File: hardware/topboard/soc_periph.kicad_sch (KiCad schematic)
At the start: 16 parts

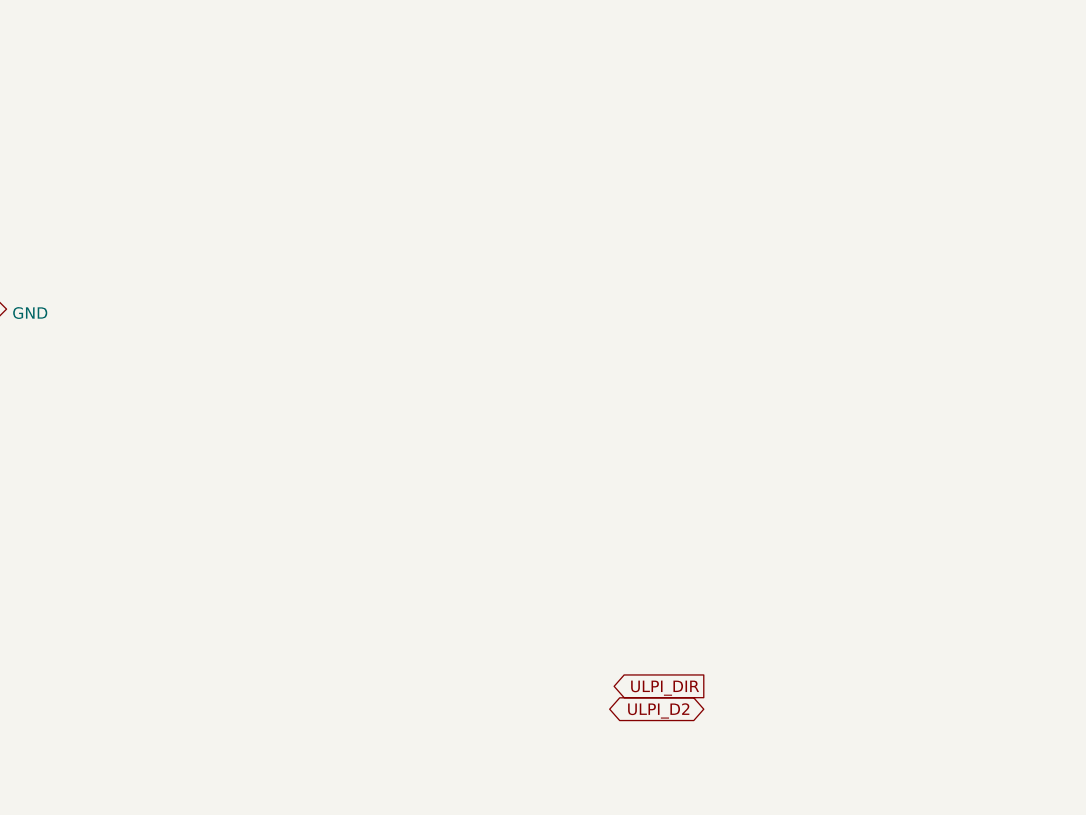
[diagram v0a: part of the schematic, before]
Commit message: Add PCIe and camera to front board
Signed-off-by: gatecat <gatecat@ds0.me>
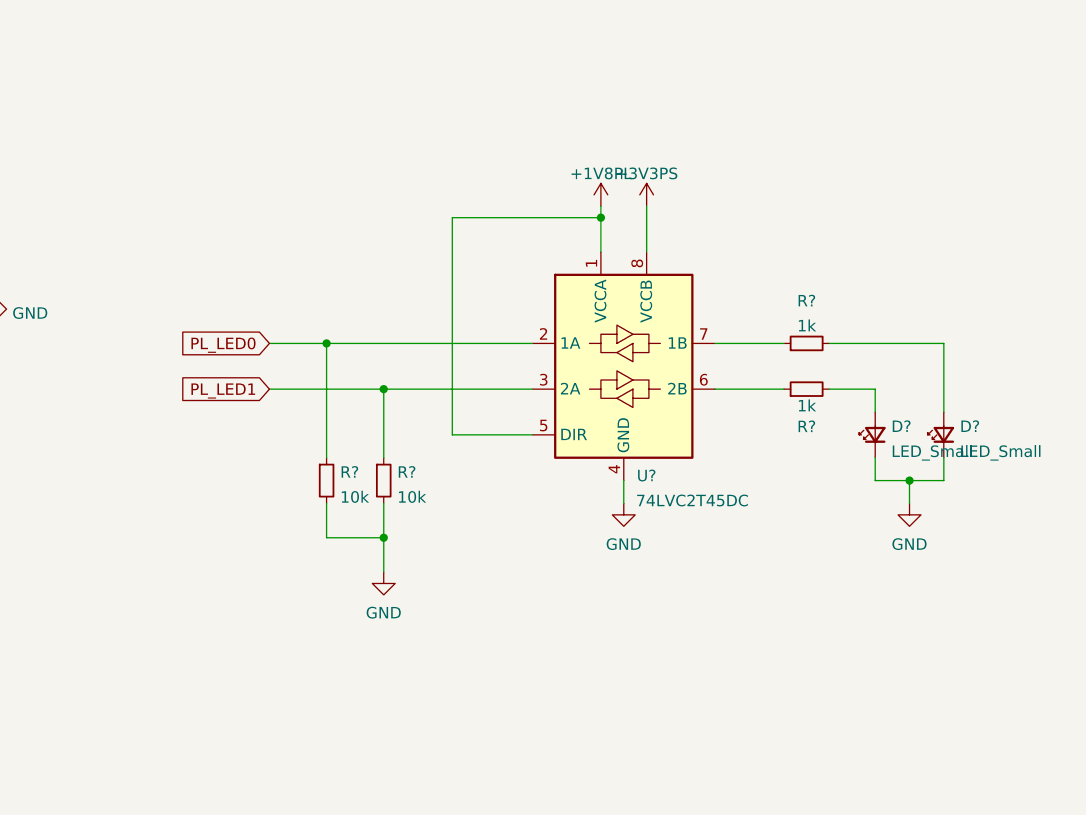
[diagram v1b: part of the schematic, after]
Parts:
- added D? (x2): LED_Small, symbol Device:LED_Small
- added R? (x2): 1k, symbol Device:R_Small
- added R? (x2): 10k, symbol Device:R_Small
- added U?: 74LVC2T45DC, Package_SO:VSSOP-8_2.3x2mm_P0.5mm, symbol Logic_LevelTranslator:74LVC2T45DC
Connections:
- net +3V3PS: now also U?.8 (VCCB)
- net GND: now also D?.1 (K), D?.1 (K), R?.2, R?.2, U?.4 (GND)
- new net: R?.1, U?.7 (1B)
- new net: D?.2 (A), R?.2 (x2)
- new net: R?.1, U?.6 (2B)
- new net +1V8PL: U?.1 (VCCA), U?.5 (DIR)
- new net PL_LED0: R?.1, U?.2 (1A)
- new net PL_LED1: R?.1, U?.3 (2A)

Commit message: Add IMU
Signed-off-by: gatecat <gatecat@ds0.me>
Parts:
- removed D? (x2): LED_Small, symbol Device:LED_Small
- removed R? (x2): 1k, symbol Device:R_Small
- removed R? (x2): 10k, symbol Device:R_Small
- removed U?: 74LVC2T45DC, Package_SO:VSSOP-8_2.3x2mm_P0.5mm, symbol Logic_LevelTranslator:74LVC2T45DC
- added C? (x3): 100n, symbol Device:C_Small
- added C?: 1µ, symbol Device:C_Small
- added D? (x7): LED_Small, symbol Device:LED_Small
- added Q? (x8): BSS138, Package_TO_SOT_SMD:SOT-23, symbol Transistor_FET:BSS138
- added R? (x11): 2.2k, symbol Device:R_Small
- added R? (x8): 10k, symbol Device:R_Small
- added U?: ICM-20789, symbol meowality:ICM-20789
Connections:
- net +1V8PL: now also R?.2
- net +1V8PS: now also C?.1, C?.1, C?.1, R?.1, R?.1, R?.2, R?.2, U?.13 (V_{DD}), U?.8 (V_{DDIO})
- net GND: now also C?.1, C?.2, C?.2, C?.2, Q?.2 (S), Q?.2 (S), Q?.2 (S), Q?.2 (S), Q?.2 (S), Q?.2 (S), Q?.2 (S), Q?.2 (S), R?.2, R?.2, R?.2, R?.2, R?.2, R?.2, R?.2, U?.18 (GND)
- net PL_LED0: now also Q?.1 (G), R?.1
- net PL_LED1: now also Q?.1 (G), R?.1
- new net: D?.2 (A), R?.1 (x7)
- new net: C?.2, U?.10 (REGOUT)
- new net: D?.1 (K), Q?.3 (D) (x7)
- new net +5V: R?.2, R?.2, R?.2, R?.2, R?.2, R?.2, R?.2
- new net I2C1_SCL: R?.2, U?.7 (PR_CL)
- new net I2C1_SDA: R?.2, U?.6 (PR_DA)
- new net IMU_FSYNC: U?.11 (FSYNC)
- new net IMU_INT: Q?.3 (D), R?.1
- new net IMU_INT_PS: Q?.1 (G), R?.1, U?.12 (INT)
- new net PS_ERR_OUT: Q?.1 (G), R?.1
- new net PS_ERR_STAT: Q?.1 (G), R?.1
- new net PS_LED: Q?.1 (G), R?.1
- new net SPI_C2M: U?.9 (AD0/SDO)
- new net SPI_M2C: U?.24 (SDA/SDI)
- new net SPI_SCLK: U?.23 (SCL/SCLK)
- new net SPI_~{CS}: R?.1, U?.22 (~{CS})
- new net VccO_EN_PL: Q?.1 (G), R?.1
- new net VccO_EN_PS: Q?.1 (G), R?.1
- no-connect marks 10 -> 18

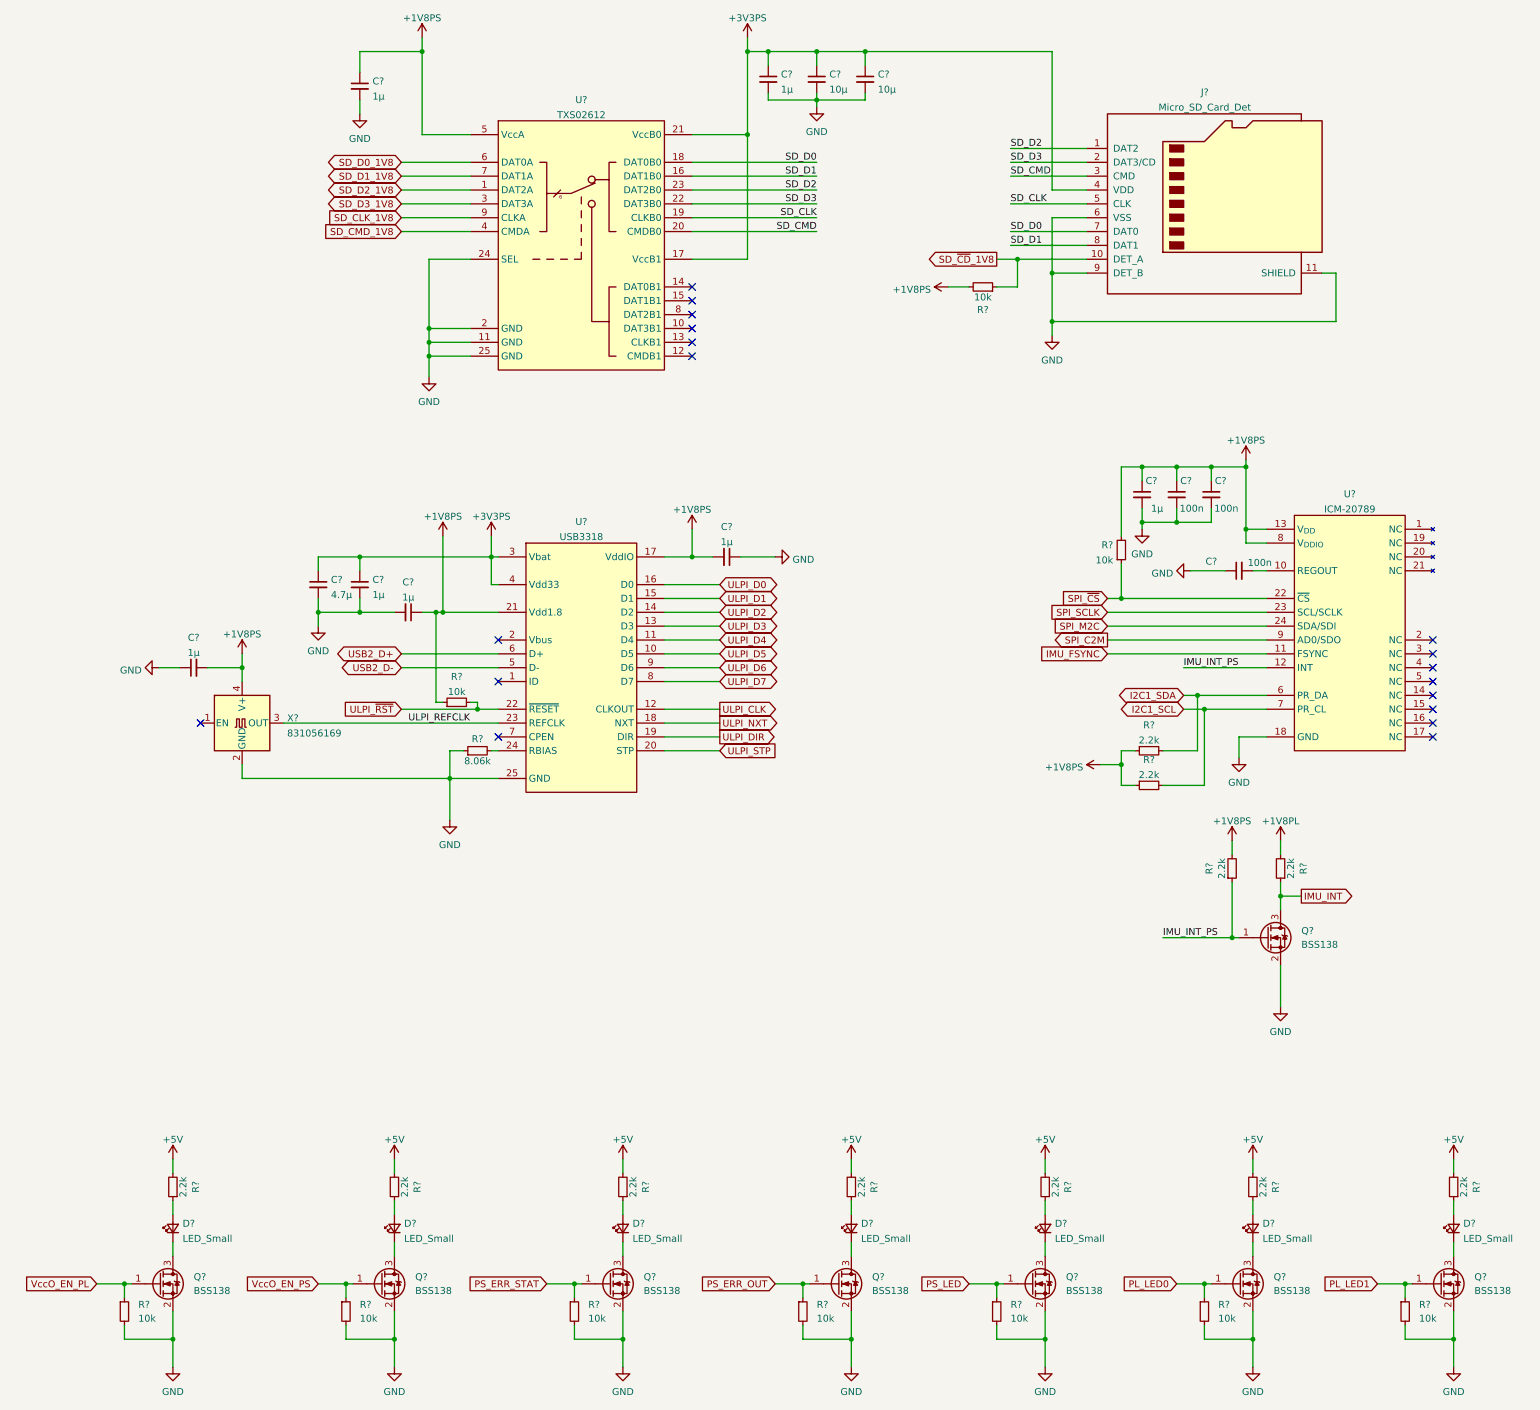
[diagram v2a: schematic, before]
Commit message: Fixing various top board issues
Signed-off-by: gatecat <gatecat@ds0.me>
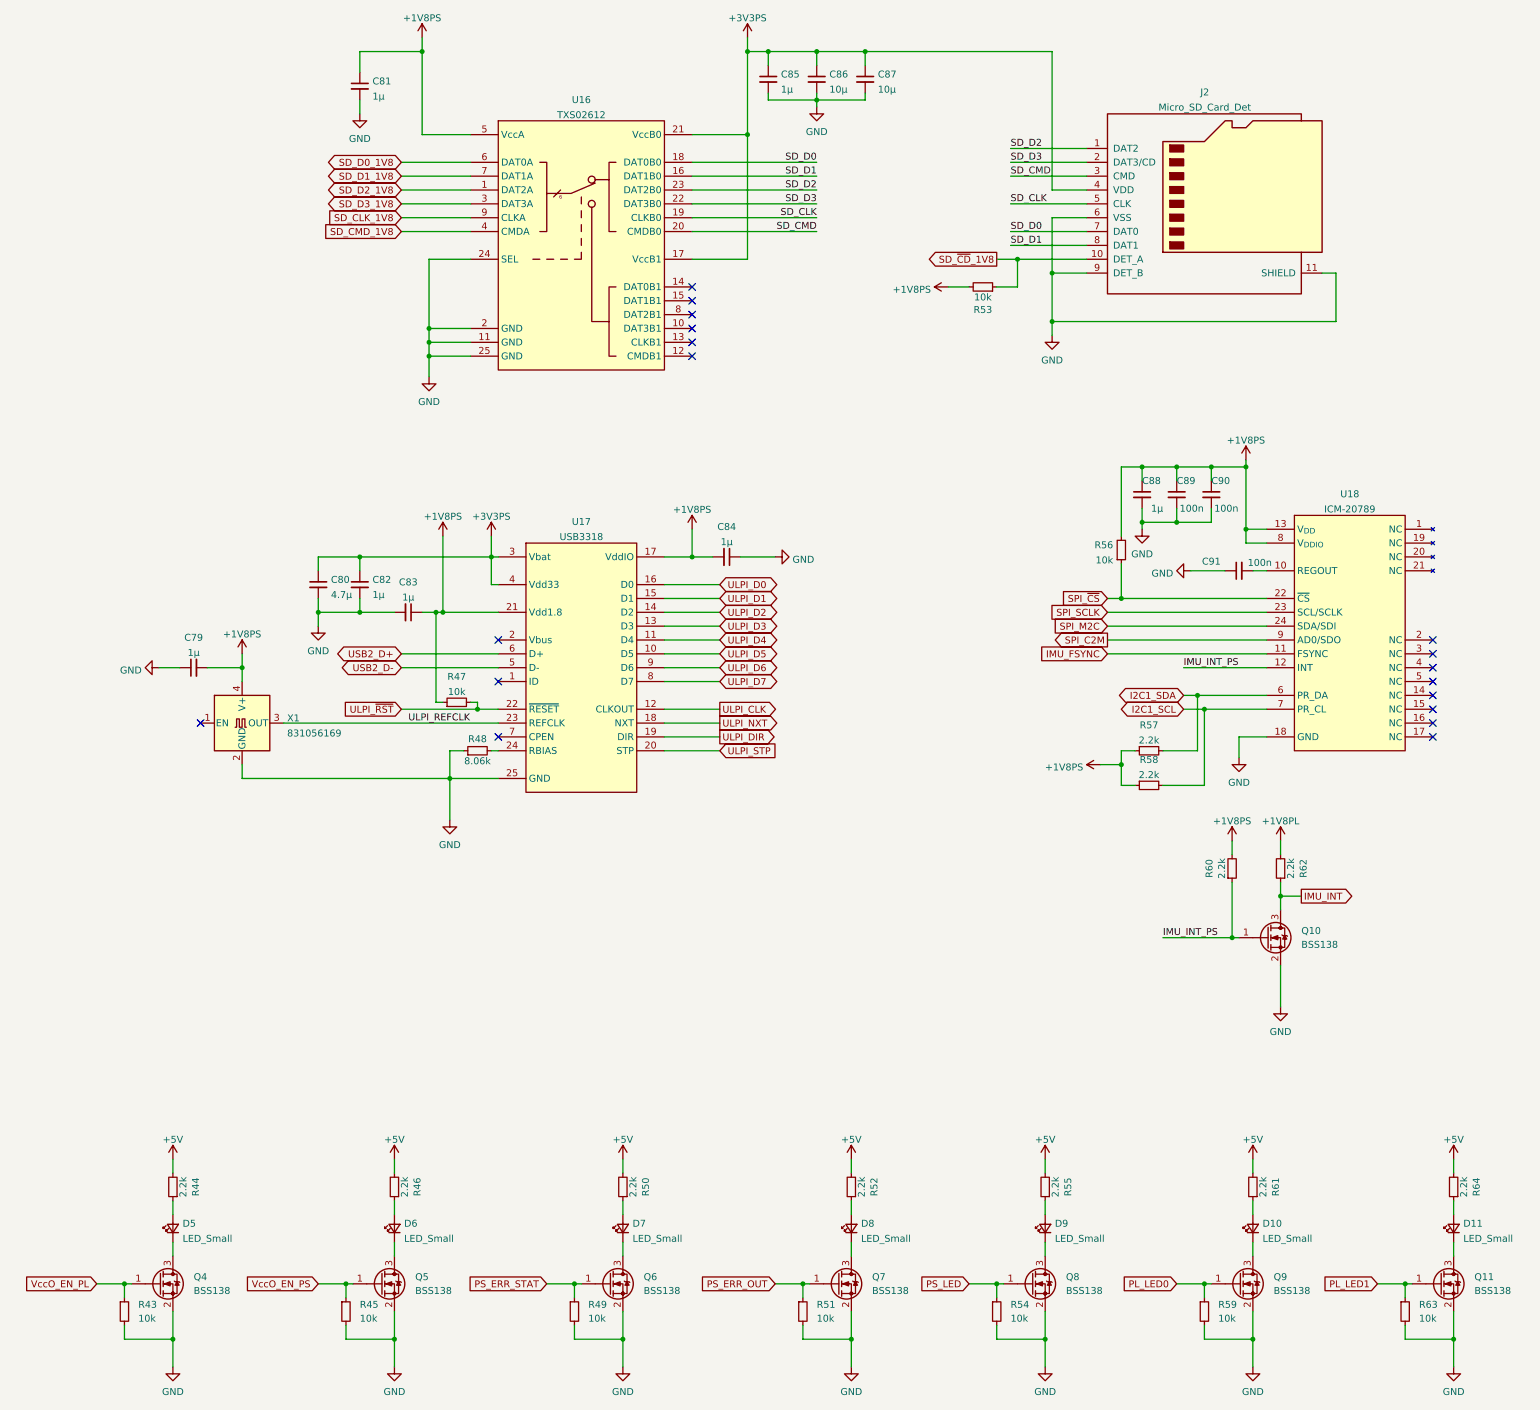
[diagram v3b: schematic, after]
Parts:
- gave numbers to parts that had none: 55

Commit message: Assign most top-board footprints
Signed-off-by: gatecat <gatecat@ds0.me>
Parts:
- C79, C81, C82, C83, C84, C85, C88: footprint (none) -> Capacitor_SMD:C_0603_1608Metric
- C80: footprint (none) -> Capacitor_SMD:C_0805_2012Metric_Pad1.15x1.40mm_HandSolder
- C86, C87: footprint (none) -> Capacitor_SMD:C_0805_2012Metric
- C89, C90, C91: footprint (none) -> Capacitor_SMD:C_0402_1005Metric
- D10, D11, D5, D6, D7, D8, D9: footprint (none) -> LED_SMD:LED_0603_1608Metric
- J2: footprint (none) -> Connector_Card:microSD_HC_Hirose_DM3AT-SF-PEJM5
- R43, R44, R45, R46, R47, R48, R49, R50, R51, R52, R53, R54, R55, R56, R57, R58, R59, R60, R61, R62, R63, R64: footprint (none) -> Resistor_SMD:R_0402_1005Metric
- U16: footprint (none) -> Package_DFN_QFN:WQFN-24-1EP_4x4mm_P0.5mm_EP2.45x2.45mm
- U17: footprint (none) -> Package_DFN_QFN:HVQFN-24-1EP_4x4mm_P0.5mm_EP2.5x2.5mm
